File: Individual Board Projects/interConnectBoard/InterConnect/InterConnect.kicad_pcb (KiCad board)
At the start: 2 copper layers, 14.5 x 30 mm, 2 parts, among them J1 5x2.54mm+2xBus, J2 5x2.54mm+2xBus

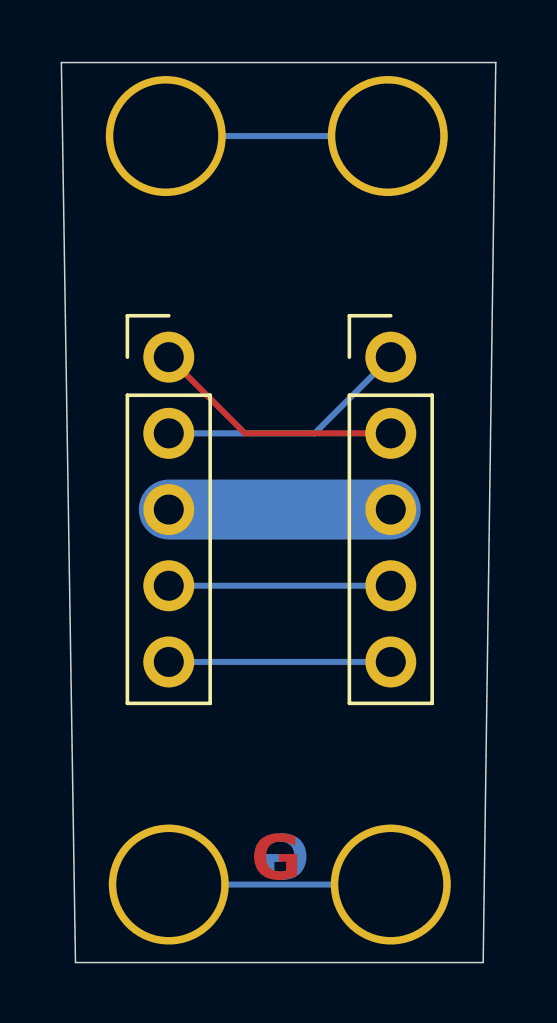
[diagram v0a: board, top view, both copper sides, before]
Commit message: Gerbers For Interconnect And Module
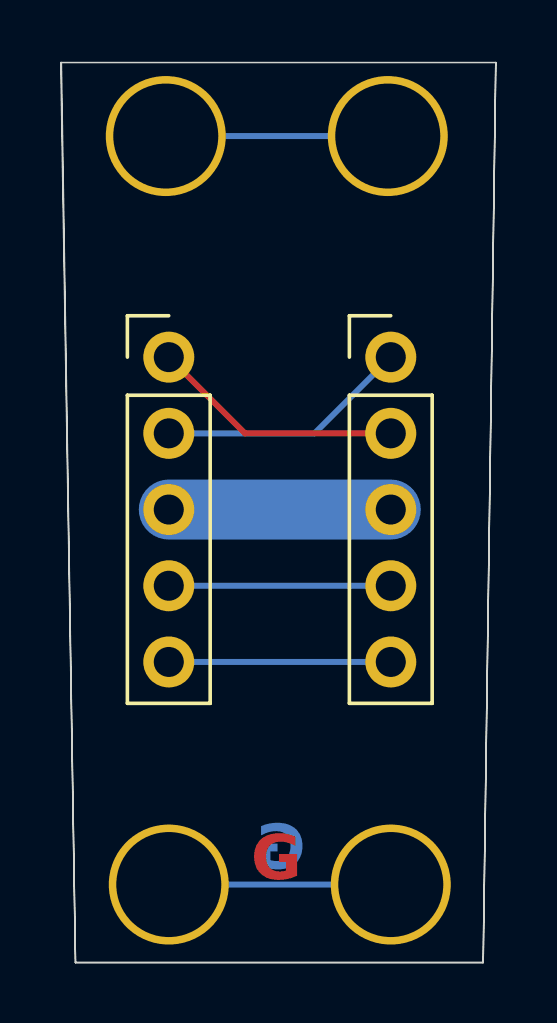
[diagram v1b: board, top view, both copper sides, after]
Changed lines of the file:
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@@
 		(tenting front back)
 		(pcbplotparams
-			(layerselection 0x00000000_00000000_55555555_5755f5ff)
+			(layerselection 0x00000000_00000000_55555555_57555555)
 			(plot_on_all_layers_selection 0x00000000_00000000_00000000_00000000)
 			(disableapertmacros no)
@@
 			(dashed_line_gap_ratio 3.000000)
 			(svgprecision 4)
-			(plotframeref no)
+			(plotframeref yes)
 			(mode 1)
 			(useauxorigin no)
@@
 			(outputformat 1)
 			(mirror no)
-			(drillshape 1)
+			(drillshape 0)
 			(scaleselection 1)
-			(outputdirectory "")
+			(outputdirectory "../../../GERBER OUTPUT FILES FOR PRODUCTION/INTERCONNECT/")
 		)
 	)
@@
 	)
 	(gr_line
-		(start 122.47 85.1)
+		(start 122.45 85.1)
 		(end 136.95 85.1)
 		(stroke
@@
 		(start 122.94 115.1)
 		(end 122.47 85.1)
+		(stroke
+			(width 0.05)
+			(type default)
+		)
+		(layer "Edge.Cuts")
+	)
+	(gr_line
+		(start 136.95 85.1)
+		(end 136.53 115.1)
+		(stroke
+			(width 0.05)
+			(type default)
+		)
+		(layer "Edge.Cuts")
+	)
+	(gr_line
+		(start 122.94 115.1)
+		(end 122.45 85.1)
+		(stroke
+			(width 0.05)
+			(type default)
+		)
+		(layer "Edge.Cuts")
+	)
+	(gr_line
+		(start 122.94 115.1)
+		(end 136.53 115.1)
 		(stroke
 			(width 0.05)
@@
 	)
 	(gr_text "G"
-		(at 130.74 112.5 0)
+		(at 130.61 112.15 0)
 		(layer "B.Cu")
 		(effects

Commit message: Controll Finished - READY TO FAB
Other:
- board size 14.5 x 30 mm -> 14.5 x 30.1 mm
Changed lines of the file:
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@@
 	)
 	(gr_line
-		(start 122.45 85.1)
-		(end 136.95 85.1)
-		(stroke
-			(width 0.05)
-			(type default)
-		)
-		(layer "Edge.Cuts")
-	)
-	(gr_line
-		(start 136.95 85.1)
+		(start 136.95 85.04)
 		(end 136.53 115.1)
 		(stroke
@@
 	)
 	(gr_line
-		(start 136.53 115.1)
-		(end 122.94 115.1)
+		(start 122.44902 85.04)
+		(end 122.45 85.1)
 		(stroke
 			(width 0.05)
@@
 	)
 	(gr_line
-		(start 122.94 115.1)
-		(end 122.47 85.1)
+		(start 125.46 85.04)
+		(end 136.95 85.04)
 		(stroke
 			(width 0.05)
@@
 	)
 	(gr_line
-		(start 136.95 85.1)
-		(end 136.53 115.1)
+		(start 125.46 85.04)
+		(end 124 85.04)
+		(stroke
+			(width 0.05)
+			(type default)
+		)
+		(layer "Edge.Cuts")
+	)
+	(gr_line
+		(start 124 85.04)
+		(end 122.44902 85.04)
 		(stroke
 			(width 0.05)
@@
 		)
 	)
+	(dimension
+		(type orthogonal)
+		(layer "Eco2.User")
+		(pts
+			(xy 125.96 86.82) (xy 125.96 84.31)
+		)
+		(height -20.14)
+		(orientation 1)
+		(format
+			(prefix "")
+			(suffix "")
+			(units 3)
+			(units_format 0)
+			(precision 4)
+			(suppress_zeroes yes)
+		)
+		(style
+			(thickness 0.1)
+			(arrow_length 1.27)
+			(text_position_mode 0)
+			(arrow_direction outward)
+			(extension_height 0.58642)
+			(extension_offset 0.5)
+			(keep_text_aligned yes)
+		)
+		(gr_text "2.51"
+			(at 104.67 85.565 90)
+			(layer "Eco2.User")
+			(effects
+				(font
+					(size 1 1)
+					(thickness 0.15)
+				)
+			)
+		)
+	)
